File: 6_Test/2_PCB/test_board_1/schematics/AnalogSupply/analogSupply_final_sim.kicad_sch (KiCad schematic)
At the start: 19 parts, among them U3 ADA4807-1AKSZ-R7

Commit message: progress on merging
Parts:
- removed C? (x2): CL10A475KP8NNNC, CAP_0603_CL10A_1P6XP8_SAM, symbol Cap4.7uF:CL10A475KP8NNNC
- removed L?: BLM18PG121SN1D, IND_BLM18_0603_MUR, symbol ferriteBeads120Ohm:BLM18PG121SN1D
- removed R7: 3310Y-001-103L, 3310Y-001-103L:TRIM_3310Y-001-103L, symbol potentiometer:3310Y-001-103L
- removed R?: RC0402JR-071KL, RC0402N_YAG, symbol Resistor1k:RC0402JR-071KL
- removed U?: TPS74501PDRVR, DRV0006A, symbol LDO:TPS74501PDRVR
- removed U?: ADA4807-1AKSZ-R7, KS-6_ADI, symbol Opamp:ADA4807-1AKSZ-R7
- removed V--1: 0, symbol Simulation_SPICE:VDC
- removed V?: 3, symbol Simulation_SPICE:VDC
- added C1, C2: CL10A475KP8NNNC, CAP_0603_CL10A_1P6XP8_SAM, symbol Cap4.7uF:CL10A475KP8NNNC
- added L1: BLM18PG121SN1D, IND_BLM18_0603_MUR, symbol ferriteBeads120Ohm:BLM18PG121SN1D
- added R1: RC0402JR-071KL, RC0402N_YAG, symbol Resistor1k:RC0402JR-071KL
- added R6: 3310Y-001-103L, 3310Y-001-103L:TRIM_3310Y-001-103L, symbol potentiometer:3310Y-001-103L
- added U1: TPS74501PDRVR, DRV0006A, symbol LDO:TPS74501PDRVR
- added U2: ADA4807-1AKSZ-R7, KS-6_ADI, symbol Opamp:ADA4807-1AKSZ-R7
- added V1: 3, symbol Simulation_SPICE:VDC
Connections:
- net AVDD: now also C3.1, R1.1, U1.1 (OUT)
- net GND: now also U3.2 (-VS), C1.2, C2.2, R6.2, U1.3 (GND), U1.7 (PAD), U2.2 (-VS), V1.2; no longer R5.2
- net VHI: now also U2.1 (VOUT), U2.4 (-IN)
- net at R4.2: now also R5.1, U2.3 (+IN); no longer R2.1
- net at R3.2: now also R2.2, U1.2 (FB)
- net at U3.5 (*DISABLE), U3.6 (+VS): now also C2.1, L1.1, U1.4 (EN), U1.6 (IN), U2.5 (*DISABLE), U2.6 (+VS)
- new net: R1.2, R2.1
- new net: R5.2, R6.1, U3.3 (+IN)
- new net: C1.1, L1.2, V1.1
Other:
- note added: "The ADC connects AVSS to GND. This jumper should only be connected for simulations"

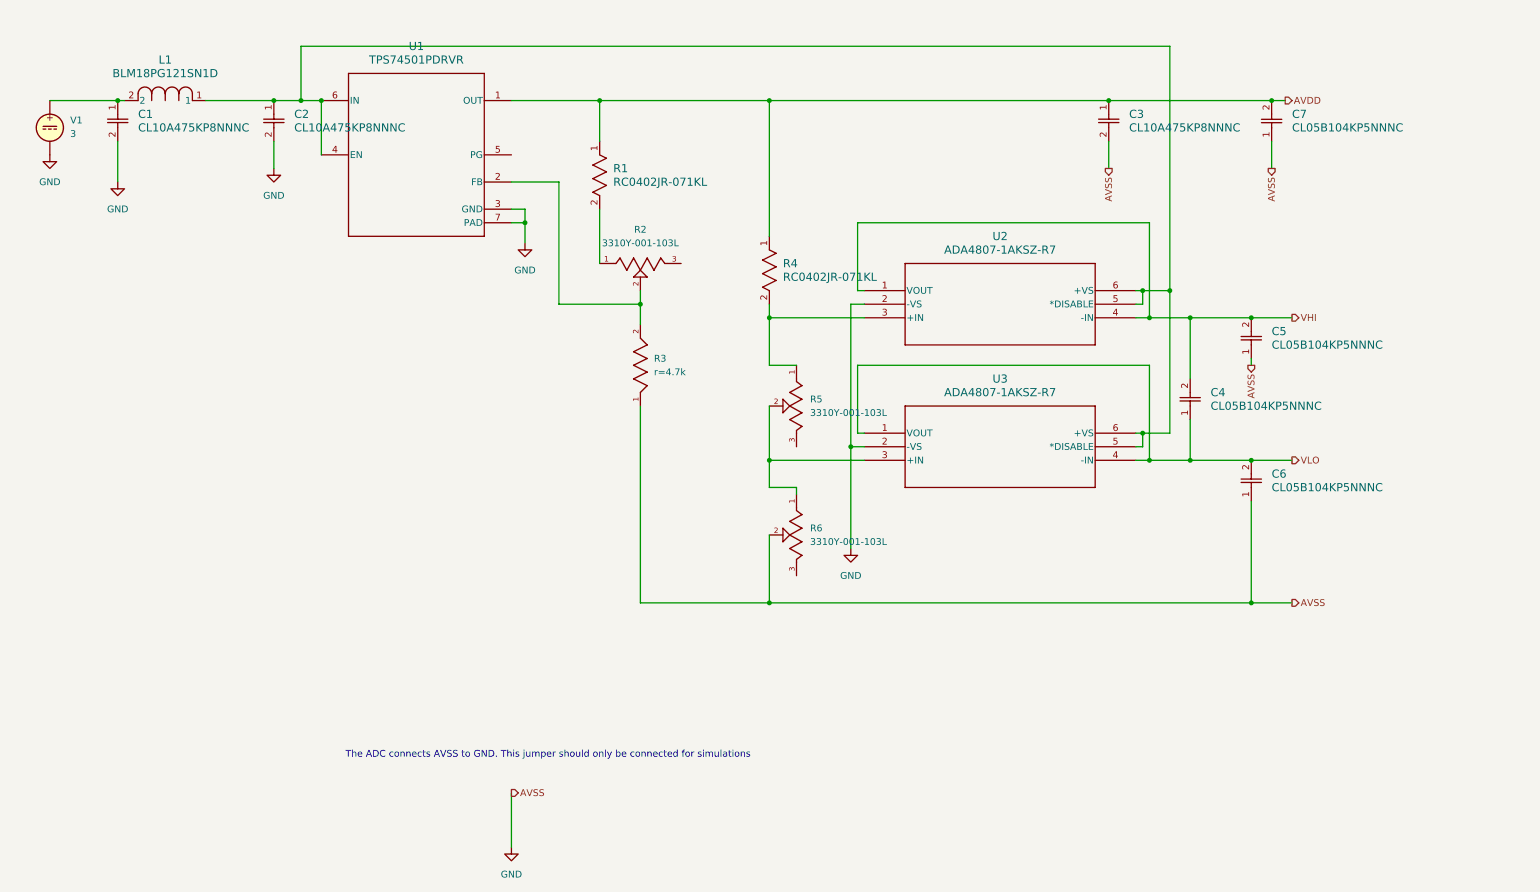
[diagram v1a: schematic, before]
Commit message: fixed digital supply, added three sheets to board main
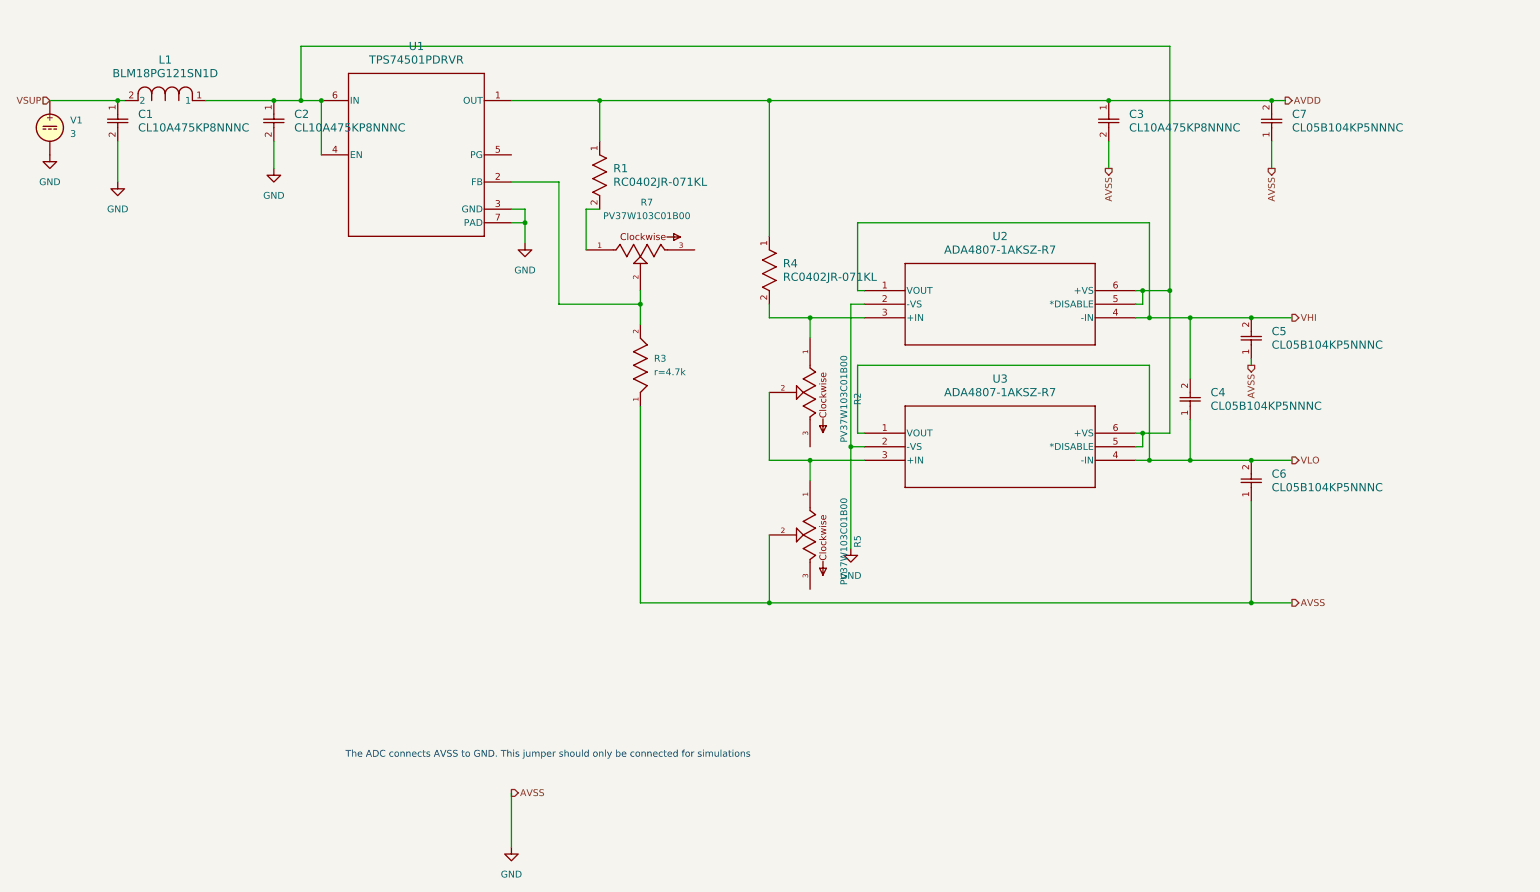
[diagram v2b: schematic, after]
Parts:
- removed R2, R5, R6: 3310Y-001-103L, 3310Y-001-103L:TRIM_3310Y-001-103L, symbol potentiometer:3310Y-001-103L
- added R2, R5, R7: PV37W103C01B00, PV37W103C01B00:TRIM_PV37W103C01B00, symbol pot_10turn:PV37W103C01B00
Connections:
- net GND: now also R5.2
- net at R4.2, U2.3 (+IN): now also R2.1
- net at R1.2: now also R7.1
- net at R3.2, U1.2 (FB): now also R7.2
- net at U3.3 (+IN): now also R2.2, R5.1
- net VSUP: now reaches C1.1, L1.2, V1.1
